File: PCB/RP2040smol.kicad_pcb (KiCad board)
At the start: 4 copper layers, 25 x 25 mm, 41 parts, among them SW1 BOOTSEL, SW2 RESET, U1 MIC5528, U2 RP2040, U3 W25Q64JVZP, Y1 Crystal_520-120-18-33JGN-TR3

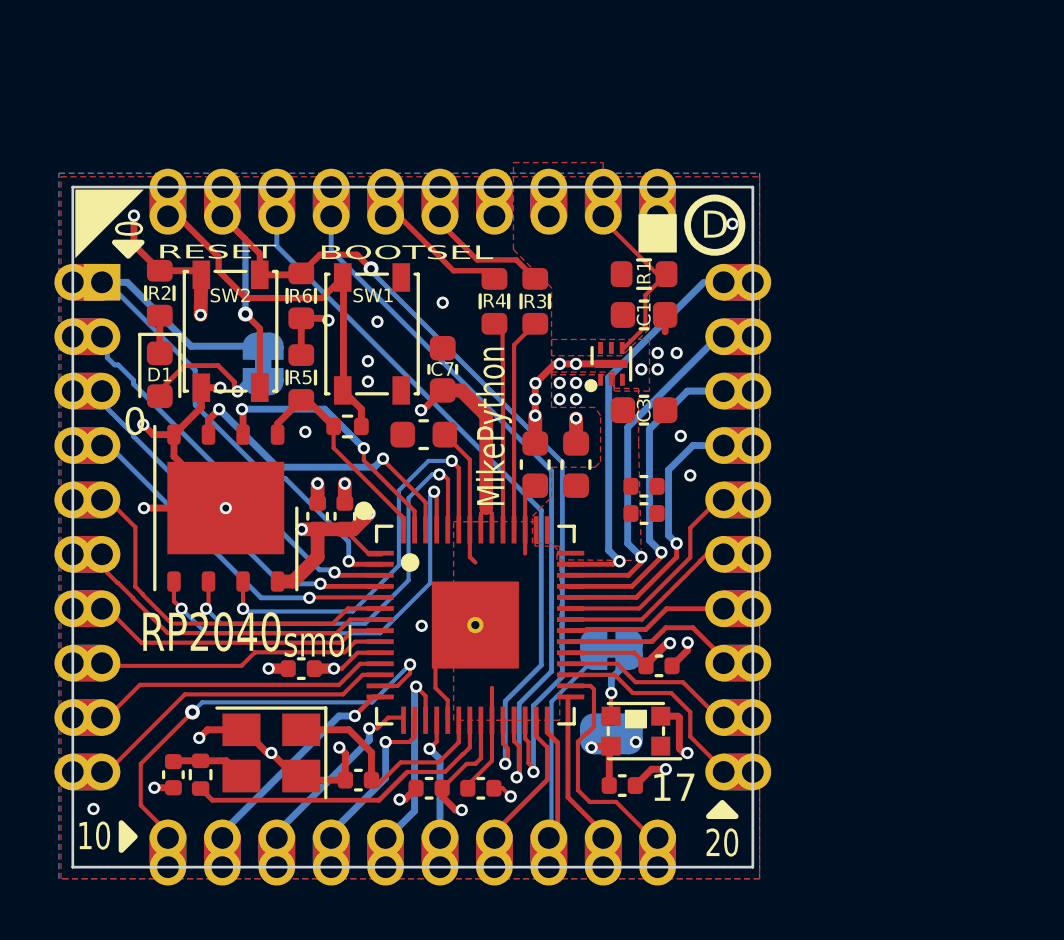
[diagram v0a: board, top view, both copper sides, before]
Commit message: RevD.
* All small passives are now 0603+
* Pads for RP2040 and MIC5528 have been extended to try to make soldering more reasonable
* Removed WS2812b capacitor. Hopefully the board has enough capacitance without it.
* Rearranged BOOTSEL and Reset buttons
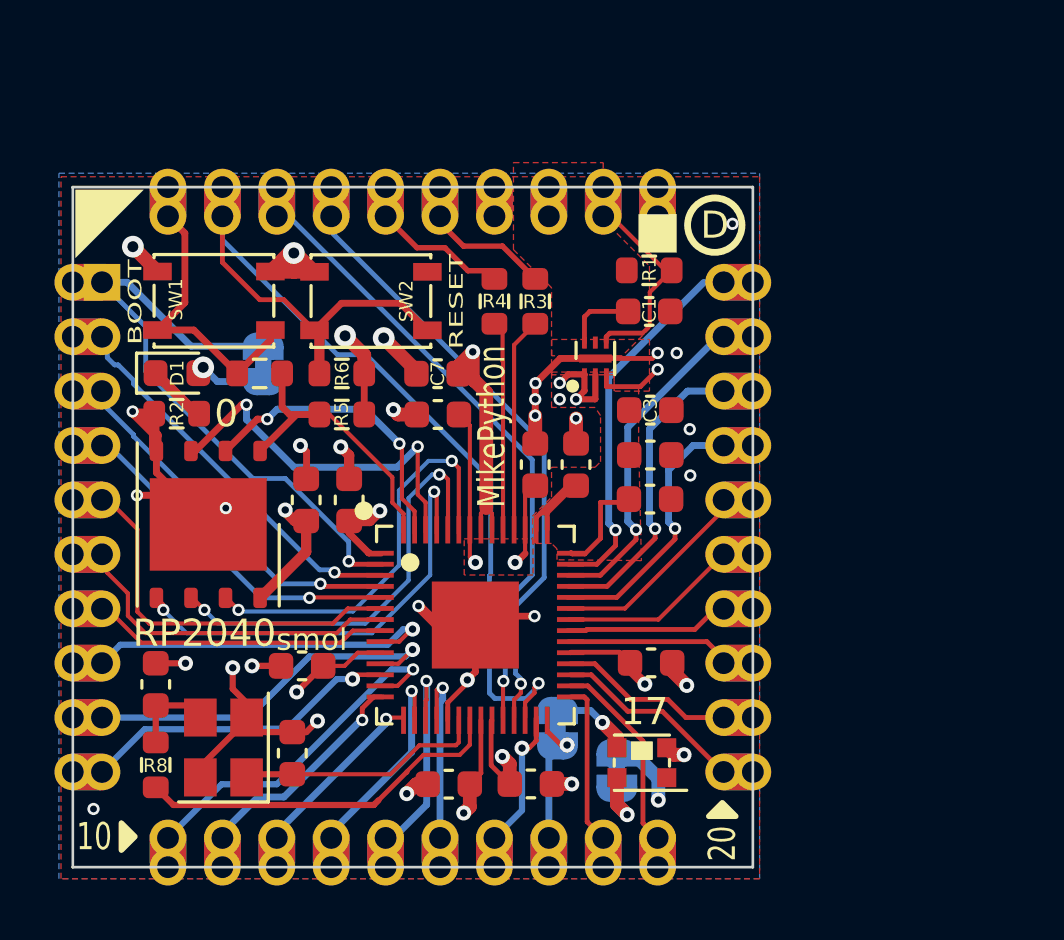
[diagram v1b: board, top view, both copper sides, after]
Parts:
- removed C14: 100nF, Capacitor_SMD:C_0402_1005Metric
- C10, C11, C13, C15, C16, C17, C4, C5, C6, C9: footprint Capacitor_SMD:C_0402_1005Metric -> Capacitor_SMD:C_0603_1608Metric
- R2: value 33 -> 330
- R3, R4: value 22 -> 27
- R7, R8: footprint Resistor_SMD:R_0402_1005Metric -> Resistor_SMD:R_0603_1608Metric
- SW1: value BOOTSEL -> BOOT
- moved SW1 5.94 mm to (131.7, 100.7), turned to 0 degrees
- moved SW2 5.28 mm to (137.5, 100.7), turned to 0 degrees
- moved R2 4.47 mm to (130.3, 104.8), turned to 0 degrees
- moved R7 3.77 mm to (133.4, 103.3), turned to 180 degrees
- moved JP2 3.50 mm to (144.3, 116.4), turned to 90 degrees
- moved C17 3.38 mm to (129.6, 114.8), turned to -90 degrees
- moved R6 3.22 mm to (136.4, 103.3), turned to 0 degrees
- moved C16 2.62 mm to (134.6, 117.3), turned to 90 degrees
- moved R5 2.02 mm to (136.4, 104.9), turned to 180 degrees
- moved C13 1.85 mm to (143.3, 118.4)
- moved Y1 1.77 mm to (132.0, 117.1), turned to 90 degrees
- moved R8 1.69 mm to (129.6, 117.7)
- moved JP1 1.36 mm to (146.5, 118.0), turned to -90 degrees
- moved D2 1.18 mm to (147.4, 117.7)
- moved C9 1.17 mm to (147.7, 106.3)
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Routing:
- net +3V3: track 30.8 -> 45.3 mm, vias 12 -> 11
- net +1V1: track 11.8 -> 23.1 mm, vias 0 -> 3
- net GND: track 40.9 -> 50.4 mm, vias 38 -> 31
- net /GPIO17: track 11.0 -> 4.00 mm, vias 0 -> 1
- net /SWDIO: track 26.8 -> 21.7 mm
- net /SWCLK: track 26.5 -> 22.6 mm
- net /BOOTSEL: track 13.6 -> 10.5 mm
- net /GPIO7: track 10.4 -> 13.3 mm, vias 0 -> 1
- net /GPIO10: track 16.0 -> 13.1 mm, vias 2 -> 1
- net /GPIO8: track 10.9 -> 13.9 mm, vias 0 -> 1
- net +5V: track 0.00 -> 2.63 mm
- net /QSPI_SS: track 7.97 -> 10.5 mm
- net /QSPI_SD2: track 11.5 -> 13.9 mm
- net /GPIO15: track 4.49 -> 6.64 mm
- net Net-(D1-Pad2): track 4.46 -> 2.42 mm
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- added copper zone on In2.Cu, net +1V1
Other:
- board text added: "Compatible with Rev D solder stencil"
- board text removed: "Compatible with Rev B solder stencil Rev D has altered pads for MIC5528 and RP2040, so will generate a slightly different solder stencil than rev B"

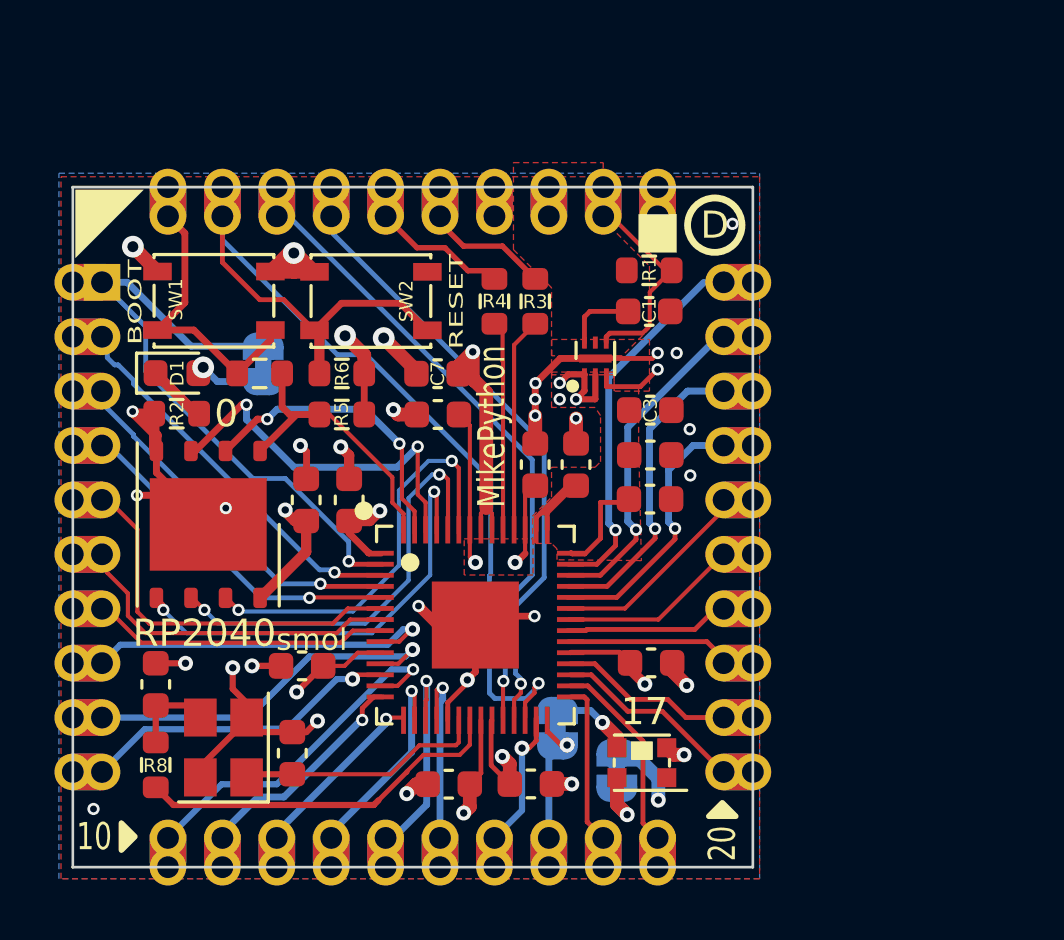
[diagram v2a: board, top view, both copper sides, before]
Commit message: * Major schematic tidy * Changed LDO to SOT23-5 AP2112K-3.3
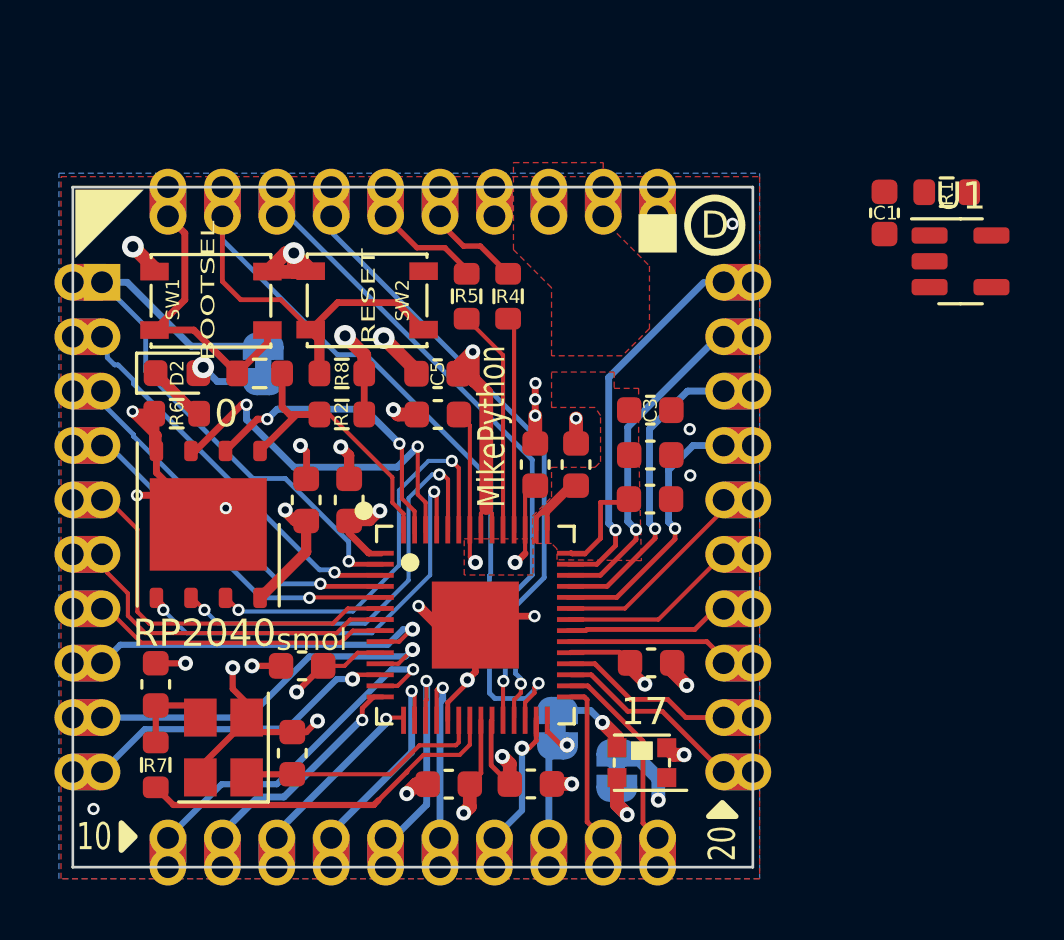
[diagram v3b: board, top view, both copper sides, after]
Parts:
- C1, C2: value 10µF -> 10u
- C10: renamed from C8; value 1uF -> 1u
- C11: renamed from C6; value 100nF -> 100n
- C12: renamed from C11; value 100nF -> 100n
- C13: renamed from C4; value 100nF -> 100n
- C14: renamed from C15; value 100nF -> 100n
- C15: renamed from C16; value 27pF -> 27p
- C16: renamed from C17; value 27pF -> 27p
- C3: value 1uF -> 1u
- C4: renamed from C10; value 100nF -> 100n
- C5: renamed from C7; value 100nF -> 100n
- C6: renamed from C5; value 100nF -> 100n
- C7: renamed from C9; value 100nF -> 100n
- C8: renamed from C13; value 100nF -> 100n
- C9: renamed from C12; value 100nF -> 100n
- R1: value 10k -> 10K
- R2: renamed from R5; value 10k -> 10K
- R3: renamed from R7; value 1k -> 1K
- R4: renamed from R3; value 27 -> 27R
- R5: renamed from R4; value 27 -> 27R
- R6: renamed from R2; value 330 -> 300R
- R7: renamed from R8; value 1k -> 1K
- R8: renamed from R6; value 10k -> 10K
- SW1: value BOOT -> BOOTSEL
- U1: value MIC5528 -> AP2112K-3.3; footprint MikeFootprintLib:MIC5528_DFN-6-1EP_1.2x1.2mm_P0.4mm_EP0.3x0.94mm_PullBack -> Package_TO_SOT_SMD:SOT-23-5
- moved U1 13.9 mm to (159.1, 99.2)
- moved R1 11.3 mm to (158.6, 96.7), turned to 0 degrees
- moved C1 9.38 mm to (156.3, 97.5), turned to -90 degrees
- moved R5 1.04 mm to (141.0, 100.5)
- moved R4 1.02 mm to (142.5, 100.5)
- moved SW2 0.14 mm to (137.3, 100.7)
- moved SW1 0.11 mm to (131.6, 100.7)
- renumbered D2 to D1, D1 to D2
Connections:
- net /USB_D+ renamed /D+
- net /USB_D- renamed /D-
- C8 pad 1: GND -> +1V1
- C8 pad 2: +1V1 -> GND
- R1 pad 1: /En -> +5V
- R1 pad 2: +5V -> Net-(R1-Pad2)
- U1 pad 1: +3V3 -> +5V
- U1 pad 2: +3V3 -> GND
- U1 pad 3: GND -> Net-(R1-Pad2)
- U1 pad 4: /En -> unconnected-(U1-Pad4)
- U1 pad 5: unconnected-(U1-Pad5) -> +3V3
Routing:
- net GND: track 50.4 -> 42.0 mm, vias 31 -> 27
- net /En: track 6.89 -> 0.00 mm
- net +3V3: track 45.3 -> 41.6 mm, vias 11 -> 8
- net +5V: track 2.63 -> 0.00 mm
- net /D-: track 4.36 -> 3.28 mm
- net /USB_DI+: track 7.38 -> 8.41 mm
- net /D+: track 4.95 -> 3.99 mm
- net +1V1: track 23.1 -> 23.8 mm, vias 3 -> 4

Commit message: E
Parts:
- MISC1: value D -> E
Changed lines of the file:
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@@
       (effects (font (size 1 1) (thickness 0.15)))
     )
-    (fp_text value "D" (at 0 0 unlocked) (layer "F.SilkS")
+    (fp_text value "E" (at 0 0 unlocked) (layer "F.SilkS")
       (effects (font (size 1 1) (thickness 0.2)))
     )

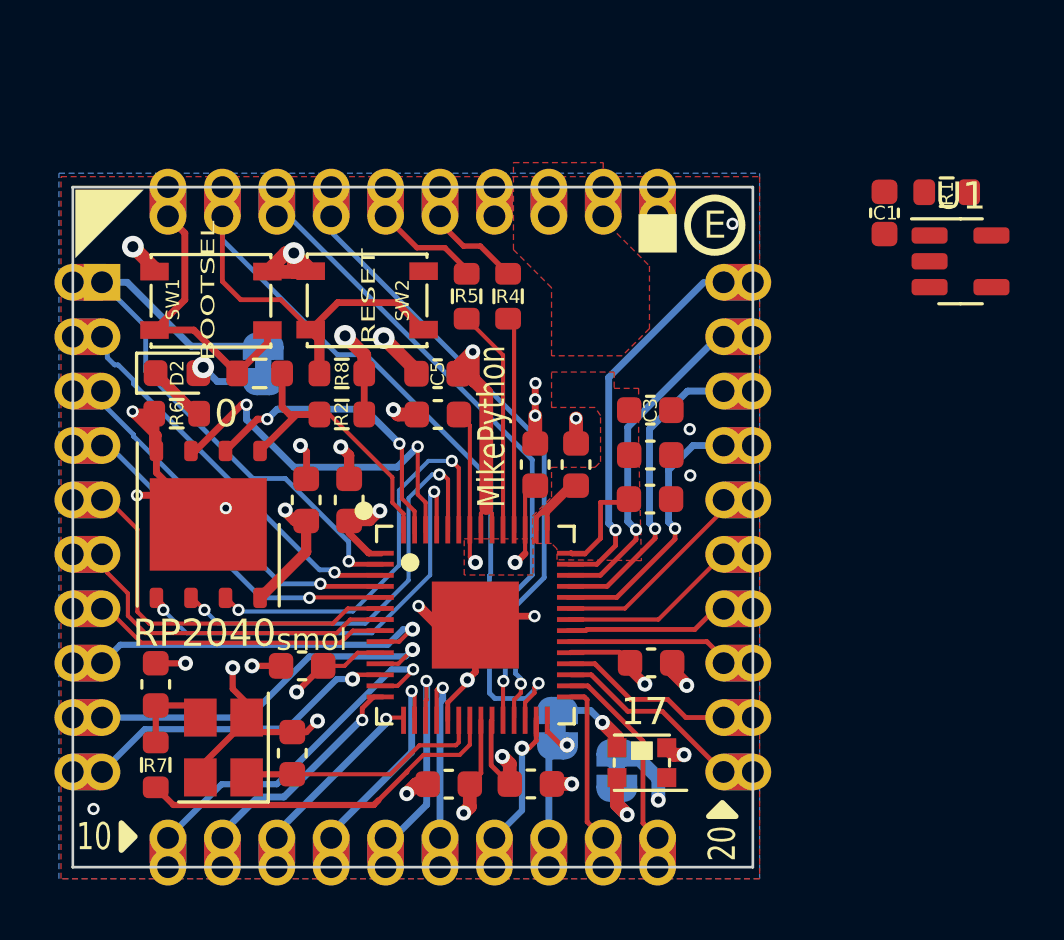
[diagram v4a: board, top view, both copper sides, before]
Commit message: Squeezed the bigger LDO onto the board...
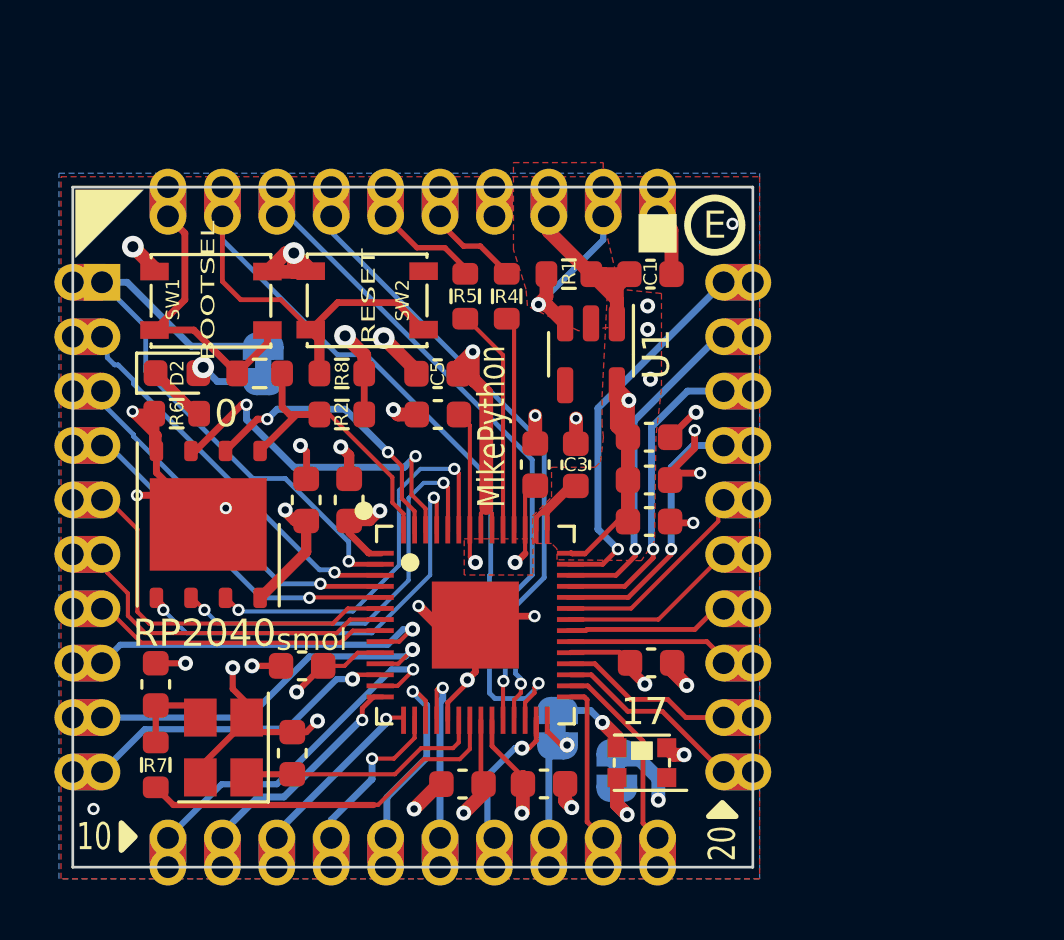
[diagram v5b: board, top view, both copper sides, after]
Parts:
- moved R1 14.2 mm to (144.7, 99.7), turned to 180 degrees
- moved U1 14.0 mm to (145.6, 102.6), turned to -90 degrees
- moved C1 8.89 mm to (147.7, 99.7), turned to 0 degrees
- moved C3 3.40 mm to (145.0, 106.7), turned to -90 degrees
- moved C2 2.87 mm to (147.7, 105.7), turned to 0 degrees
- moved C7 0.92 mm to (147.7, 107.3)
- moved C6 0.82 mm to (147.7, 108.8)
- moved C11 0.51 mm to (140.8, 118.4)
- moved C8 0.48 mm to (143.8, 118.4)
- moved R4 0.05 mm to (142.5, 100.5)
- moved R5 0.05 mm to (140.9, 100.5)
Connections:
- C8 pad 1: +1V1 -> GND
- C8 pad 2: GND -> +1V1
- R1 pad 2: Net-(R1-Pad2) -> /En
- U1 pad 3: Net-(R1-Pad2) -> /En
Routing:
- net +5V: track 0.00 -> 9.49 mm
- net GND: track 42.0 -> 50.2 mm, vias 27 -> 28
- net /En: track 0.00 -> 6.73 mm, vias 0 -> 1
- net +3V3: track 41.6 -> 47.8 mm, vias 8 -> 12
- net +1V1: track 23.8 -> 25.9 mm, vias 4 -> 3
- net /GPIO13: track 7.45 -> 5.97 mm
- net /GPIO29_ADC3: track 13.3 -> 14.6 mm

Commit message: m
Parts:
- SW1, SW2: footprint Button_Switch_SMD:SW_SPST_PTS810 -> MikeSwitchFootprints:SW_Push_SPST_Alps_SKRK_Clone
- moved SW1 15.7 mm to (130.6, 116.4), turned to 90 degrees
- moved SW2 12.1 mm to (130.6, 110.7), turned to 90 degrees
- moved R7 10.9 mm to (140.4, 117.7), turned to -90 degrees
- moved R6 8.71 mm to (133.2, 113.1), turned to 90 degrees
- moved C14 8.52 mm to (138.8, 100.4), turned to -90 degrees
- moved U3 7.81 mm to (134.3, 101.6), turned to 0 degrees
- moved D2 7.25 mm to (133.2, 110.0), turned to 90 degrees
- moved R8 6.88 mm to (130.7, 107.2)
- moved JP3 4.90 mm to (135.5, 107.5), turned to 180 degrees
- moved C16 4.59 mm to (133.1, 117.7)
- moved C15 4.34 mm to (138.9, 117.7), turned to -90 degrees
- moved Y1 4.00 mm to (136.0, 117.5), turned to 180 degrees
- moved R3 3.19 mm to (133.0, 106.5), turned to -90 degrees
- moved C10 2.89 mm to (143.4, 103.8)
- moved C3 2.77 mm to (147.7, 106.1), turned to 180 degrees
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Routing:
- net /BOOTSEL: track 10.7 -> 25.3 mm
- net GND: track 50.2 -> 38.7 mm, vias 28 -> 35
- net /XOUT: track 13.9 -> 2.48 mm
- net /QSPI_SD0: track 15.8 -> 5.04 mm, vias 2 -> 0
- net +1V1: track 25.9 -> 15.8 mm, vias 3 -> 2
- net /QSPI_SCLK: track 15.4 -> 6.48 mm, vias 2 -> 0
- net /GPIO0: track 22.4 -> 15.5 mm
- net /QSPI_SD3: track 14.8 -> 8.02 mm, vias 2 -> 0
- net /QSPI_SS: track 10.5 -> 15.7 mm
- net Net-(C16-Pad2): track 3.18 -> 8.05 mm
- net /GPIO17: track 4.00 -> 8.50 mm, vias 1 -> 0
- net /XIN: track 9.08 -> 4.91 mm
- net /QSPI_SD1: track 10.6 -> 14.1 mm, vias 2 -> 0
- net +5V: track 9.49 -> 12.4 mm
- net /GPIO29_ADC3: track 14.6 -> 11.7 mm
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- removed copper zone on F.Cu, net +1V1
- removed copper zone on F.Cu, net +5V
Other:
- board text added: "Compatible with Rev E solder stencil"
- board text removed: "Compatible with Rev D solder stencil"

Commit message: Tidied front silks
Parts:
- moved ART1 1.42 mm to (133.9, 113.5)
- moved R8 0.52 mm to (130.6, 106.7)
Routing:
- net GND: track 38.7 -> 35.5 mm
- net +5V: track 12.4 -> 9.60 mm
- net +3V3: track 49.5 -> 47.3 mm
- net /BOOTSEL: track 25.3 -> 23.5 mm
- net /RUN: track 36.7 -> 35.7 mm, vias 3 -> 1
- net /GPIO0: track 15.5 -> 14.8 mm
- net /GPIO17: track 8.50 -> 7.96 mm
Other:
- board text added: "Jan22"
- board text removed: "Dec21"
